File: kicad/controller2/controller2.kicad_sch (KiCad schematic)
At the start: 78 parts, among them J1 Conn_01x07_Male, J2 Conn_01x07_Male, J3 Conn_01x07_Male, J4 Conn_01x07_Male, U1 BluePill_STM32F103C, U2 LM324

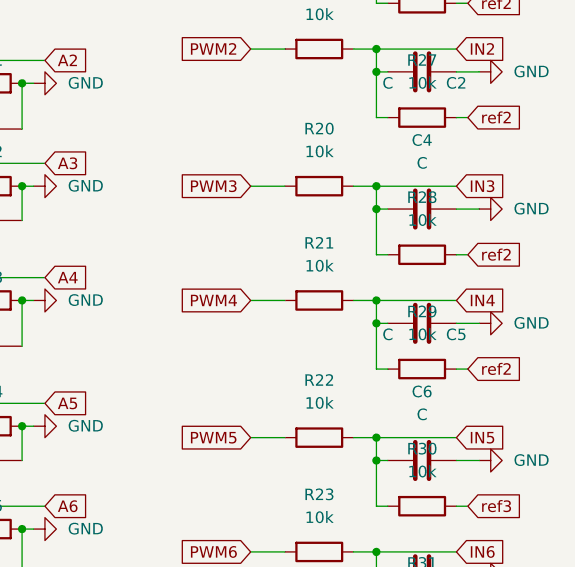
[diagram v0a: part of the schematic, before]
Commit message: fix resistor values around transistor
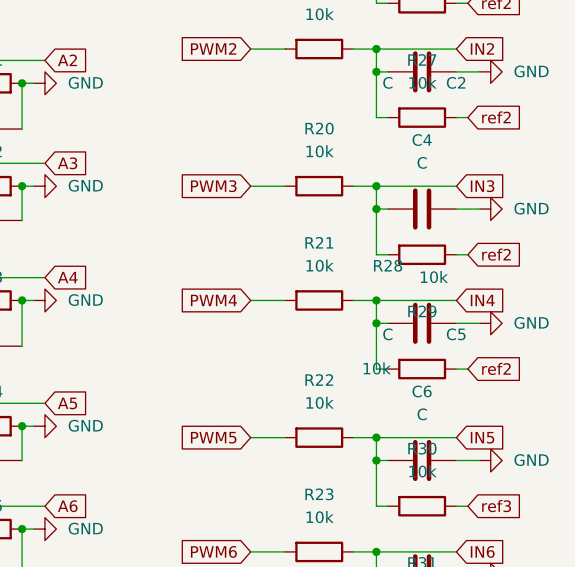
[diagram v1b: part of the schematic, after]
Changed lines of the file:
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@@
   )
   (symbol (lib_id "Device:R") (at 259.08 58.42 270) (unit 1)
-    (in_bom yes) (on_board yes) (fields_autoplaced)
-    (property "Reference" "R28" (id 0) (at 259.08 52.07 90))
-    (property "Value" "10k" (id 1) (at 259.08 54.61 90))
+    (in_bom yes) (on_board yes)
+    (property "Reference" "R28" (id 0) (at 255.27 59.69 90))
+    (property "Value" "10k" (id 1) (at 260.35 60.96 90))
     (property "Footprint" "Resistor_SMD:R_1206_3216Metric" (id 2) (at 259.08 56.642 90)
       (effects (font (size 1.27 1.27)) hide)
@@
   )
   (symbol (lib_id "Device:R") (at 259.08 71.12 270) (unit 1)
-    (in_bom yes) (on_board yes) (fields_autoplaced)
+    (in_bom yes) (on_board yes)
     (property "Reference" "R29" (id 0) (at 259.08 64.77 90))
-    (property "Value" "10k" (id 1) (at 259.08 67.31 90))
+    (property "Value" "10k" (id 1) (at 254 71.12 90))
     (property "Footprint" "Resistor_SMD:R_1206_3216Metric" (id 2) (at 259.08 69.342 90)
       (effects (font (size 1.27 1.27)) hide)
